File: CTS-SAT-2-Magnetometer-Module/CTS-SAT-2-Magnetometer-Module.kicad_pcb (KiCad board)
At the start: 2 copper layers, 31 parts, among them J1 PicoBlade, J2 SWD, U1 MMC5983MA, U2 LIS2MDL, U3 STM32F072C8Tx, U4 MIC5365-3.3YD5

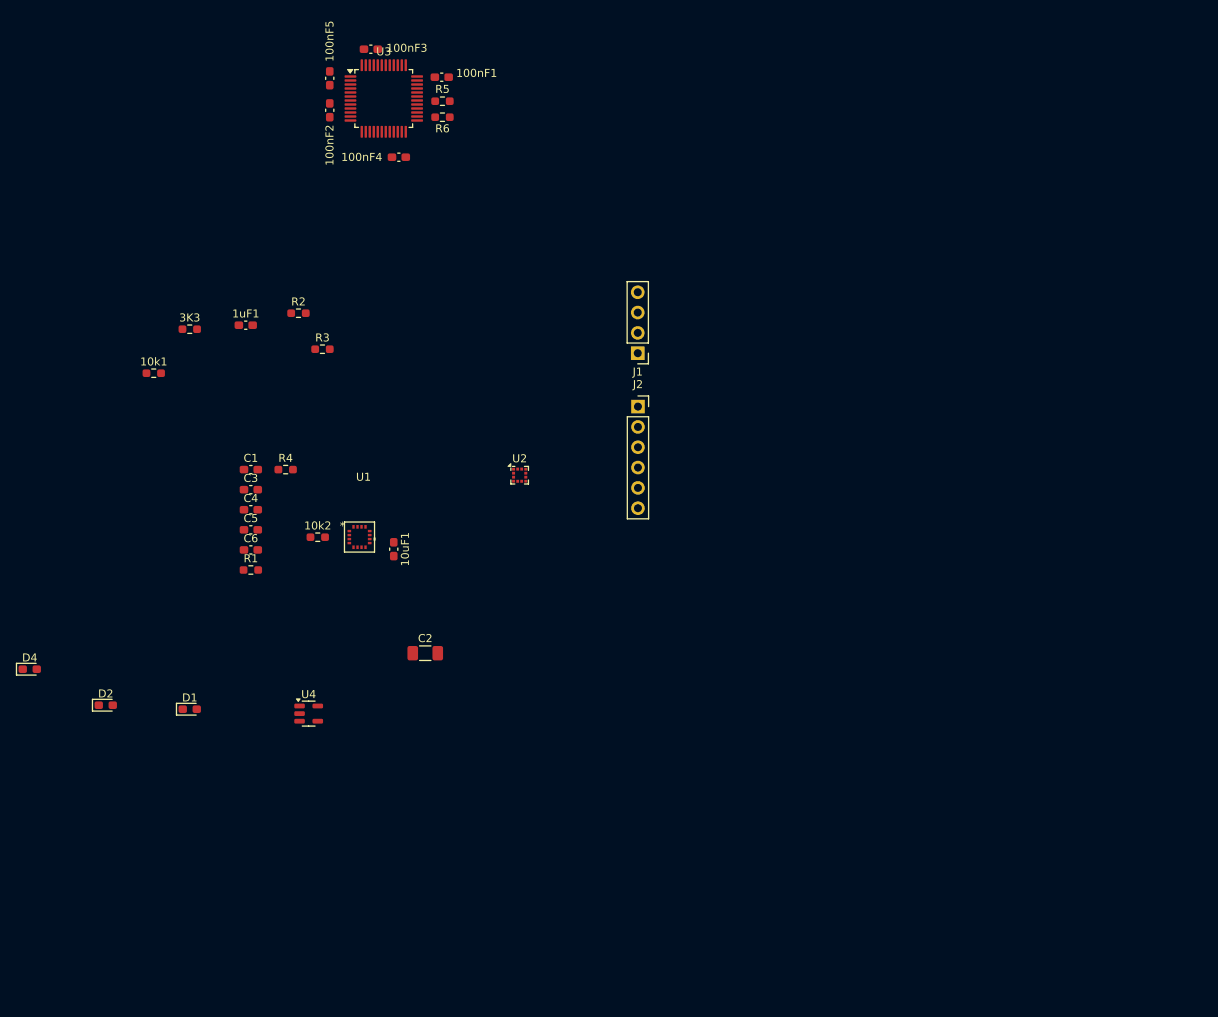
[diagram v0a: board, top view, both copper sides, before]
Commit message: Started PCB Routing
Still need to figure out how to do routing for communication lines
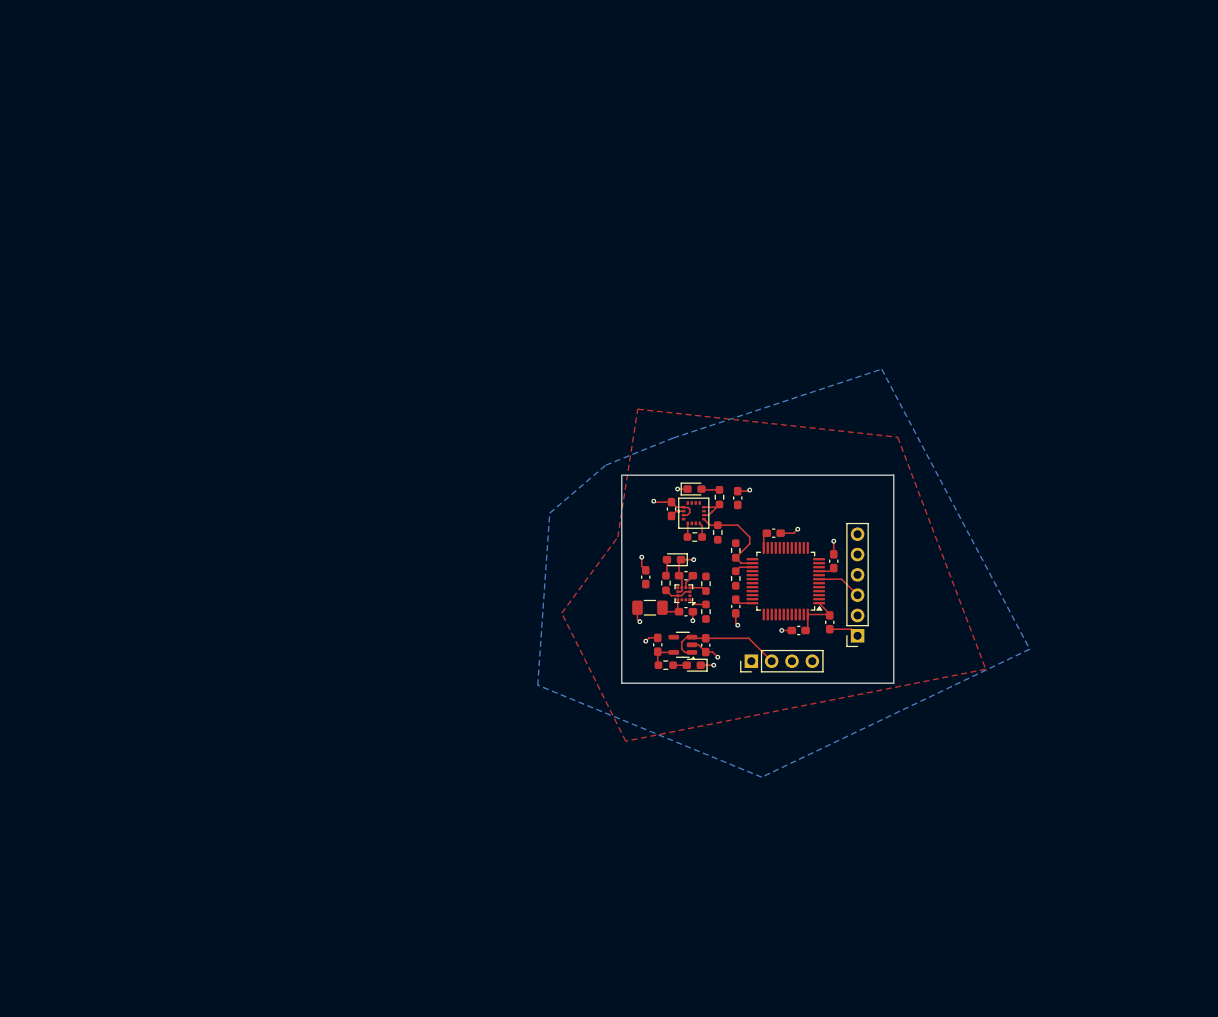
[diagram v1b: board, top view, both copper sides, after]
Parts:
- moved 100nF5 92.4 mm to (210.5, 113.1)
- moved 100nF3 90.2 mm to (206.6, 114.2), turned to 0 degrees
- moved D4 86.1 mm to (193.6, 96.5)
- moved 100nF2 84.5 mm to (211.0, 105.5)
- moved U3 78.5 mm to (205.0, 108.0), turned to 180 degrees
- moved 100nF1 75.7 mm to (198.8, 111.2), turned to 90 degrees
- moved D2 73.7 mm to (193.5, 118.5), turned to 180 degrees
- moved 10k1 73.3 mm to (196.5, 101.9), turned to 90 degrees
- moved R5 70.0 mm to (198.8, 107.7), turned to 90 degrees
- moved 3K3 69.5 mm to (196.7, 97.5), turned to 90 degrees
- moved 100nF4 66.4 mm to (203.5, 102.0), turned to 180 degrees
- moved R6 65.4 mm to (198.8, 104.2), turned to -90 degrees
- moved 1uF1 65.2 mm to (199.0, 97.6), turned to 90 degrees
- moved R2 63.6 mm to (190.0, 118.5)
- moved D1 63.3 mm to (191.0, 105.3), turned to 180 degrees
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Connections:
- 10k1 pad 1: +3V3 -> +3.3V
- 10k2 pad 2: +3V3 -> +3.3V
- 1uF1 pad 1: +3V3 -> +3.3V
- 3K3 pad 1: +3V3 -> +3.3V
- U1 pad 13: +3V3 -> +3.3V
- U1 pad 2: +3V3 -> +3.3V
- U1 pad 4: +3V3 -> +3.3V
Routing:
- net GND: track 0.00 -> 37.5 mm, vias 0 -> 14
- net +3.3V: track 0.00 -> 30.8 mm
- net SCL: track 0.00 -> 15.2 mm
- net Vdd: track 0.00 -> 15.1 mm
- net SDA: track 0.00 -> 6.36 mm
- net RESET: track 0.00 -> 5.64 mm
- net Net-(D1-A): track 0.00 -> 2.05 mm
- net Net-(U2-C1): track 0.00 -> 1.85 mm
- net Net-(U1-CAP): track 0.00 -> 1.75 mm
- net Net-(D4-A): track 0.00 -> 1.75 mm
- net Net-(D2-A): track 0.00 -> 1.71 mm
- added copper zone on F.Cu, net +3.3V
- added copper zone on B.Cu, net GND
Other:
- board outline added: 34 x 26 mm

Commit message: PCB Completed with Labels
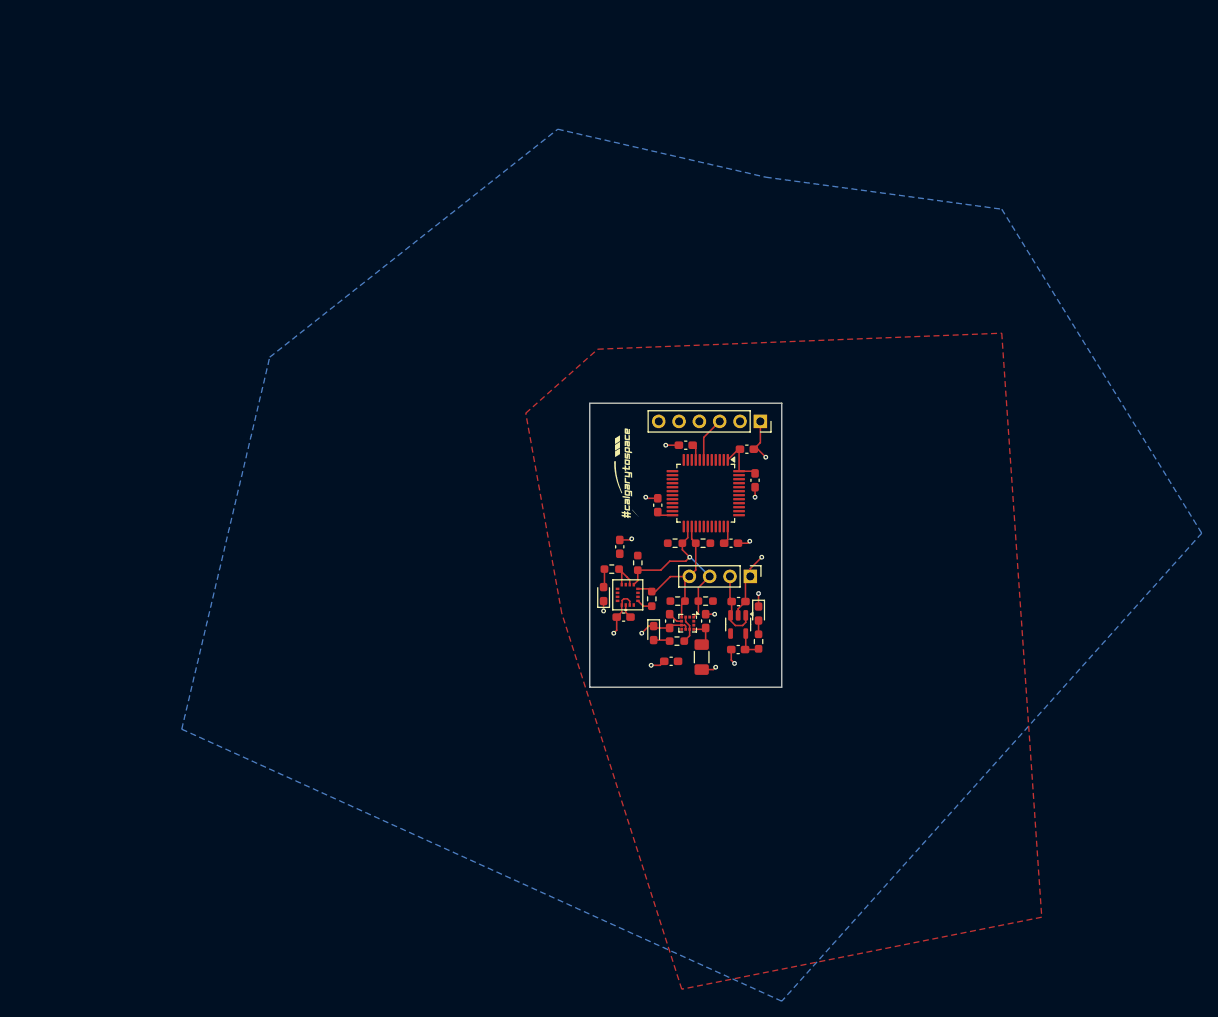
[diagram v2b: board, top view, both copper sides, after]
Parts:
- added G***: LOGO, LOGO, F.Cu at (185.0, 94.5)
- moved J2 29.4 mm to (201.8, 88.0), turned to -90 degrees
- moved 100nF5 24.0 mm to (200.1, 91.5), turned to 0 degrees
- moved 100nF2 23.5 mm to (192.5, 91.0), turned to 0 degrees
- moved 100nF3 19.6 mm to (201.2, 95.4), turned to 90 degrees
- moved D4 17.4 mm to (182.2, 109.6), turned to 90 degrees
- moved 3K3 16.2 mm to (183.2, 106.5), turned to 180 degrees
- moved 1uF1 16.0 mm to (184.2, 103.7)
- moved 100nF4 14.9 mm to (189.0, 98.5), turned to -90 degrees
- moved U3 14.9 mm to (195.0, 97.0), turned to -90 degrees
- moved 10uF1 14.8 mm to (184.7, 112.5), turned to 180 degrees
- moved U1 13.1 mm to (185.2, 109.7), turned to -90 degrees
- moved R2 12.0 mm to (201.6, 115.5), turned to 90 degrees
- moved C1 11.0 mm to (190.7, 118.0), turned to 0 degrees
- moved 10k1 10.7 mm to (186.5, 105.7), turned to -90 degrees
- moved J1 10.6 mm to (200.6, 107.4), turned to -90 degrees
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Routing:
- net SDA: track 6.36 -> 20.5 mm
- net SCL: track 15.2 -> 24.0 mm, vias 0 -> 1
- net Vdd: track 15.1 -> 8.21 mm
- net GND: track 37.5 -> 43.7 mm, vias 14 -> 15
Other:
- board size 34 x 26 mm -> 24 x 35.5 mm
- board text added: "GND"
- board text added: "Magnetometer Dev Board"
- board text added: "Marian Abebe"
- board text added: "RESET"
- board text added: "Rev2.0"
- board text added: "SCL"
- board text added: "SDA"
- board text added: "SWDCLK"
- board text added: "SWDIO"
- board text added: "VCC"
- board text added: "VDD"

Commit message: Changed one of the footprints
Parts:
- J2: footprint Connector_PinSocket_2.54mm:PinSocket_1x06_P2.54mm_Vertical -> Connector_PinSocket_2.54mm:PinSocket_1x05_P2.54mm_Vertical
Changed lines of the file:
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@@
 		)
 	)
-	(footprint "Connector_PinSocket_2.54mm:PinSocket_1x06_P2.54mm_Vertical"
+	(footprint "Connector_PinSocket_2.54mm:PinSocket_1x05_P2.54mm_Vertical"
 		(layer "F.Cu")
 		(at 201.825 88.025 -90)
-		(descr "Through hole straight socket strip, 1x06, 2.54mm pitch, single row (from Kicad 4.0.7), script generated")
-		(tags "Through hole socket strip THT 1x06 2.54mm single row")
+		(descr "Through hole straight socket strip, 1x05, 2.54mm pitch, single row (from Kicad 4.0.7), script generated")
+		(tags "Through hole socket strip THT 1x05 2.54mm single row")
 		(property "Reference" "J2"
-			(at 0 -2.77 90)
+			(at 0 -2.77 -90)
 			(layer "F.SilkS")
 			(hide yes)
@@
 		)
 		(property "Value" "SWD"
-			(at 0 15.47 90)
-			(layer "F.Fab")
-			(hide yes)
+			(at 0 12.93 -90)
+			(layer "F.Fab")
 			(effects
 				(font
@@
 			)
 		)
-		(property "Footprint" "Connector_PinSocket_2.54mm:PinSocket_1x06_P2.54mm_Vertical"
+		(property "Footprint" "Connector_PinSocket_2.54mm:PinSocket_1x05_P2.54mm_Vertical"
 			(at 0 0 -90)
 			(unlocked yes)
@@
 		(attr through_hole)
 		(fp_line
-			(start -1.33 14.03)
-			(end 1.33 14.03)
+			(start -1.33 11.49)
+			(end 1.33 11.49)
 			(stroke
 				(width 0.12)
@@
 		(fp_line
 			(start -1.33 1.27)
-			(end -1.33 14.03)
+			(end -1.33 11.49)
 			(stroke
 				(width 0.12)
@@
 		(fp_line
 			(start 1.33 1.27)
-			(end 1.33 14.03)
+			(end 1.33 11.49)
 			(stroke
 				(width 0.12)
@@
 		)
 		(fp_line
-			(start -1.8 14.45)
+			(start -1.8 11.9)
 			(end -1.8 -1.8)
 			(stroke
@@
 		)
 		(fp_line
-			(start 1.75 14.45)
-			(end -1.8 14.45)
+			(start 1.75 11.9)
+			(end -1.8 11.9)
 			(stroke
 				(width 0.05)
@@
 		(fp_line
 			(start 1.75 -1.8)
-			(end 1.75 14.45)
-			(stroke
-				(width 0.05)
-				(type solid)
-			)
-			(layer "F.CrtYd")
-		)
-		(fp_line
-			(start -1.27 13.97)
+			(end 1.75 11.9)
+			(stroke
+				(width 0.05)
+				(type solid)
+			)
+			(layer "F.CrtYd")
+		)
+		(fp_line
+			(start -1.27 11.43)
 			(end -1.27 -1.27)
 			(stroke
@@
 		)
 		(fp_line
-			(start 1.27 13.97)
-			(end -1.27 13.97)
+			(start 1.27 11.43)
+			(end -1.27 11.43)
 			(stroke
 				(width 0.1)
@@
 		(fp_line
 			(start 1.27 -0.635)
-			(end 1.27 13.97)
+			(end 1.27 11.43)
 			(stroke
 				(width 0.1)
@@
 			(layer "F.Fab")
 		)
+		(fp_text user "${REFERENCE}"
+			(at 0 5.08 0)
+			(layer "F.Fab")
+			(effects
+				(font
+					(size 1 1)
+					(thickness 0.15)
+				)
+			)
+		)
 		(pad "1" thru_hole rect
 			(at 0 0 270)
@@
 			(pintype "passive")
 		)
-		(pad "6" thru_hole oval
-			(at 0 12.7 270)
-			(size 1.7 1.7)
-			(drill 1)
-			(layers "*.Cu" "*.Mask")
-			(remove_unused_layers no)
-		)
-		(model "${KICAD8_3DMODEL_DIR}/Connector_PinSocket_2.54mm.3dshapes/PinSocket_1x06_P2.54mm_Vertical.wrl"
+		(model "${KICAD8_3DMODEL_DIR}/Connector_PinSocket_2.54mm.3dshapes/PinSocket_1x05_P2.54mm_Vertical.wrl"
 			(offset
 				(xyz 0 0 0)
